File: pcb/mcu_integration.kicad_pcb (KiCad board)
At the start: 4 copper layers, 100 x 100 mm, 104 parts, among them IC1 TL7660IDGKR, IC10 AD844_OPAMP_MEL, IC2 TL081IDT, IC3 FOD814_OPTO_NOSHD, IC4 UA78M33CDCYG3, IC5 FOD814_OPTO_MEL, IC6 AD844_OPAMP_AL, IC7 FOD814_OPTO_AL, IC8 AD844_OPAMP_NOSHD, J1 Micro_SD_Card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

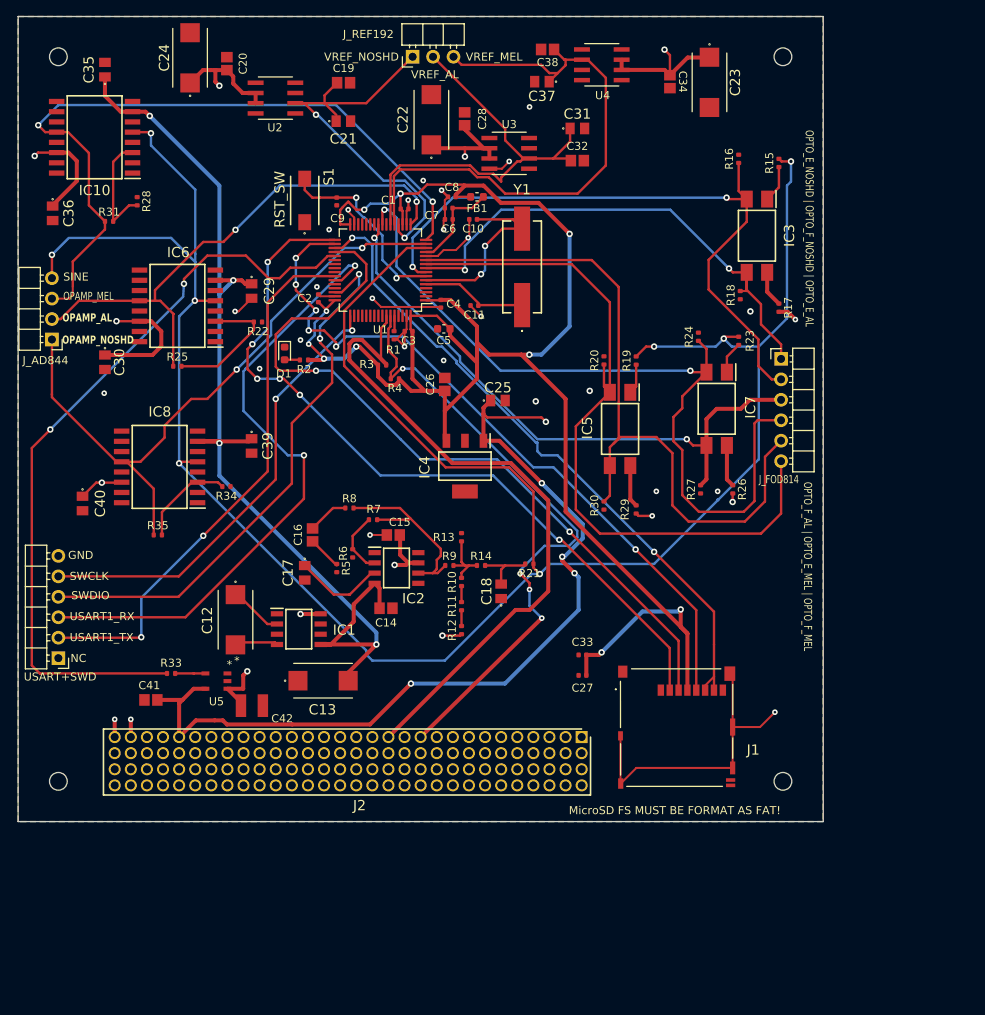
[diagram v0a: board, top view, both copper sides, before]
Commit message: Karim start 2nd rev (#16)
* done layout/ratsnet

* 95% of second rev done, just two errors
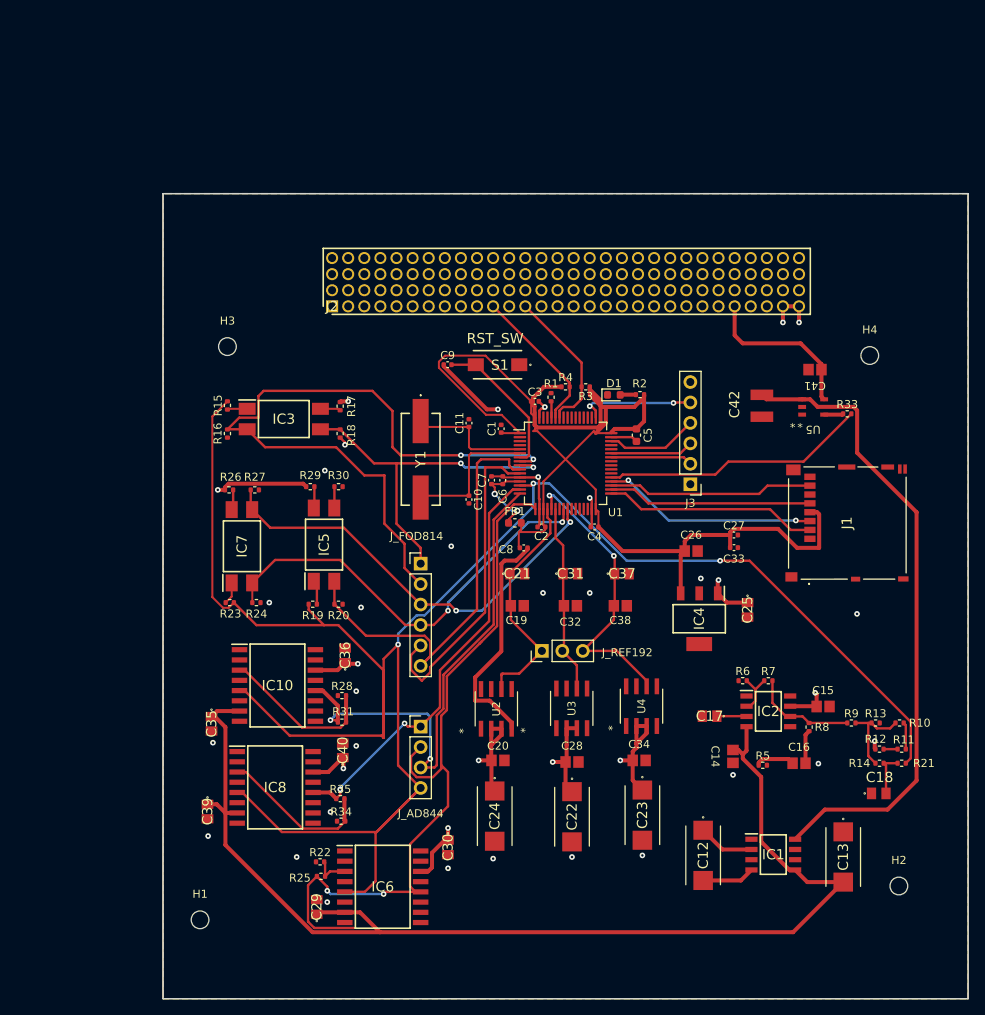
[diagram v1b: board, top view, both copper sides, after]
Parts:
- J3, J_FOD814: footprint Connector_PinHeader_2.54mm:PinHeader_1x06_P2.54mm_Horizontal -> Connector_PinHeader_2.54mm:PinHeader_1x06_P2.54mm_Vertical
- J_AD844: footprint Connector_PinHeader_2.54mm:PinHeader_1x04_P2.54mm_Horizontal -> Connector_PinHeader_2.54mm:PinHeader_1x04_P2.54mm_Vertical
- J_REF192: footprint Connector_PinHeader_2.54mm:PinHeader_1x03_P2.54mm_Horizontal -> Connector_PinHeader_2.54mm:PinHeader_1x03_P2.54mm_Vertical
- moved C24 101.5 mm to (124.2, 134.3), turned to -90 degrees
- moved C20 92.9 mm to (124.6, 127.4), turned to 0 degrees
- moved C41 92.1 mm to (164.0, 78.9)
- moved C23 91.4 mm to (142.5, 134.2)
- moved R33 90.0 mm to (168.0, 84.3), turned to 0 degrees
- moved C22 88.3 mm to (133.8, 134.4), turned to -90 degrees
- moved C34 84.4 mm to (142.1, 127.4), turned to 0 degrees
- moved C35 82.3 mm to (89.0, 122.8), turned to -90 degrees
- moved U5 81.6 mm to (163.8, 83.5), turned to 0 degrees
- moved J3 81.4 mm to (148.5, 93.1)
- moved C28 81.0 mm to (133.8, 127.6), turned to 0 degrees
- moved U2 80.7 mm to (124.4, 121.0), turned to 90 degrees
- moved U4 79.8 mm to (142.4, 120.7), turned to 90 degrees
- moved C29 76.9 mm to (102.1, 145.6), turned to 90 degrees
- moved IC6 76.5 mm to (110.3, 143.1), turned to 0 degrees
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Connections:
- C42 pad 1: +5V -> MOSFET_OUTPUT
- IC1 pad 8: +5V -> MOSFET_OUTPUT
- IC3 pad 3: GND -> ADC1_IN11_OPTO_E_NOSHD
- J1 pad 6: /SPI2_MISO -> GND
- J_FOD814 pad 1: GND -> ADC1_IN11_OPTO_E_NOSHD
- R18 pad 2: GND -> ADC1_IN11_OPTO_E_NOSHD
- U1 pad 9: GND -> ADC1_IN11_OPTO_E_NOSHD
- U5 pad 1: +5V -> MOSFET_OUTPUT
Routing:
- net +5V: track 240.4 -> 104.0 mm, vias 18 -> 11
- net GND: track 189.4 -> 67.4 mm, vias 29 -> 28
- net MOSFET_OUTPUT: track 0.00 -> 79.8 mm
- net /SPI2_CS_NSS: track 95.8 -> 26.5 mm, vias 6 -> 0
- net /USART1_RX: track 79.4 -> 10.3 mm, vias 2 -> 0
- net /SPI2_MOSI: track 94.9 -> 26.8 mm
- net OBC_I2C_SCL: track 85.4 -> 18.6 mm
- net /SPI2_SCK: track 89.8 -> 25.4 mm, vias 6 -> 0
- net MOSFET_CONTROL: track 95.3 -> 33.1 mm, vias 2 -> 0
- net OBC_I2C_SDA: track 78.4 -> 18.5 mm, vias 4 -> 0
- net 3.3V Output: track 218.9 -> 160.5 mm, vias 10 -> 0
- net /SWDIO: track 69.6 -> 11.4 mm, vias 2 -> 0
- net /USART1_TX: track 68.1 -> 10.2 mm, vias 2 -> 0
- net /SPI2_MISO: track 82.2 -> 25.5 mm, vias 2 -> 0
- net ADC1_IN13_OPTO_E_MEL: track 89.4 -> 42.5 mm
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- removed copper zone on In1.Cu, net GND
- removed copper zone on In2.Cu, net GND

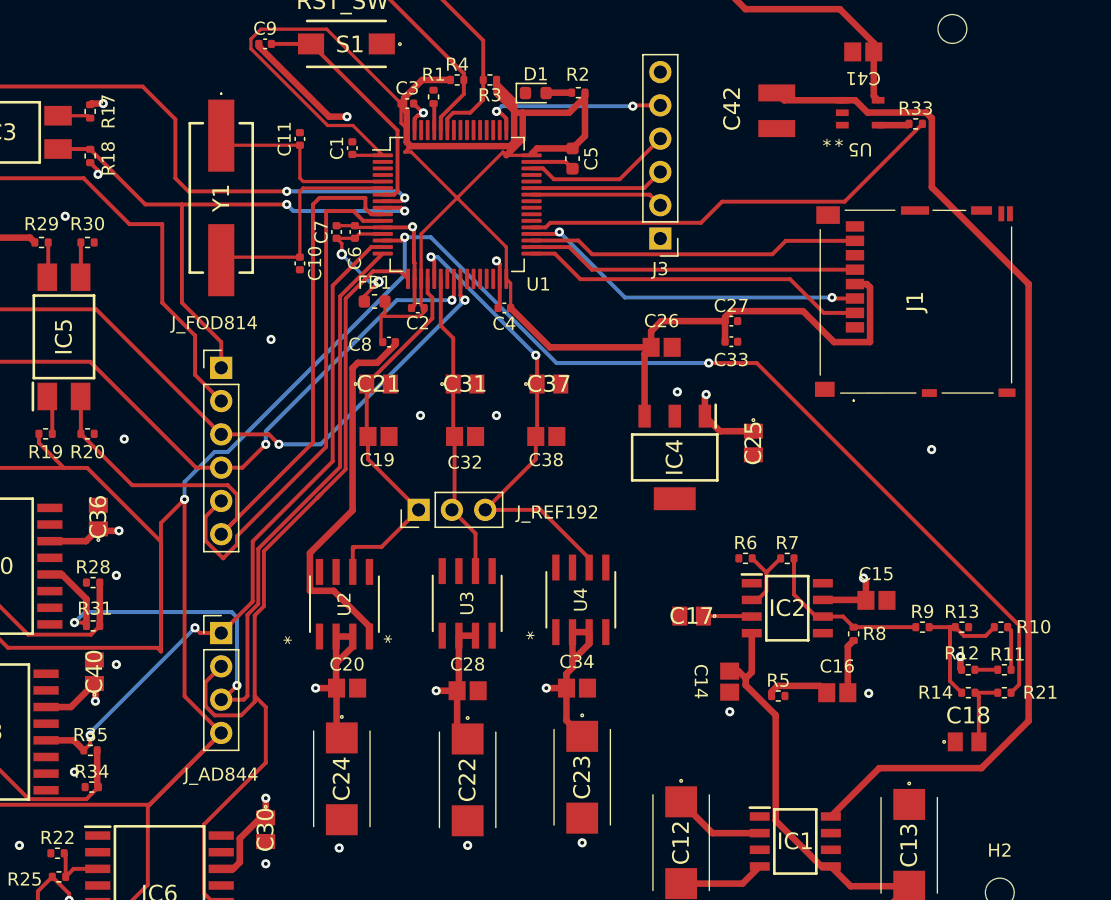
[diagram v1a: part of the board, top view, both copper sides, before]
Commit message: fix +5v connection, make final via
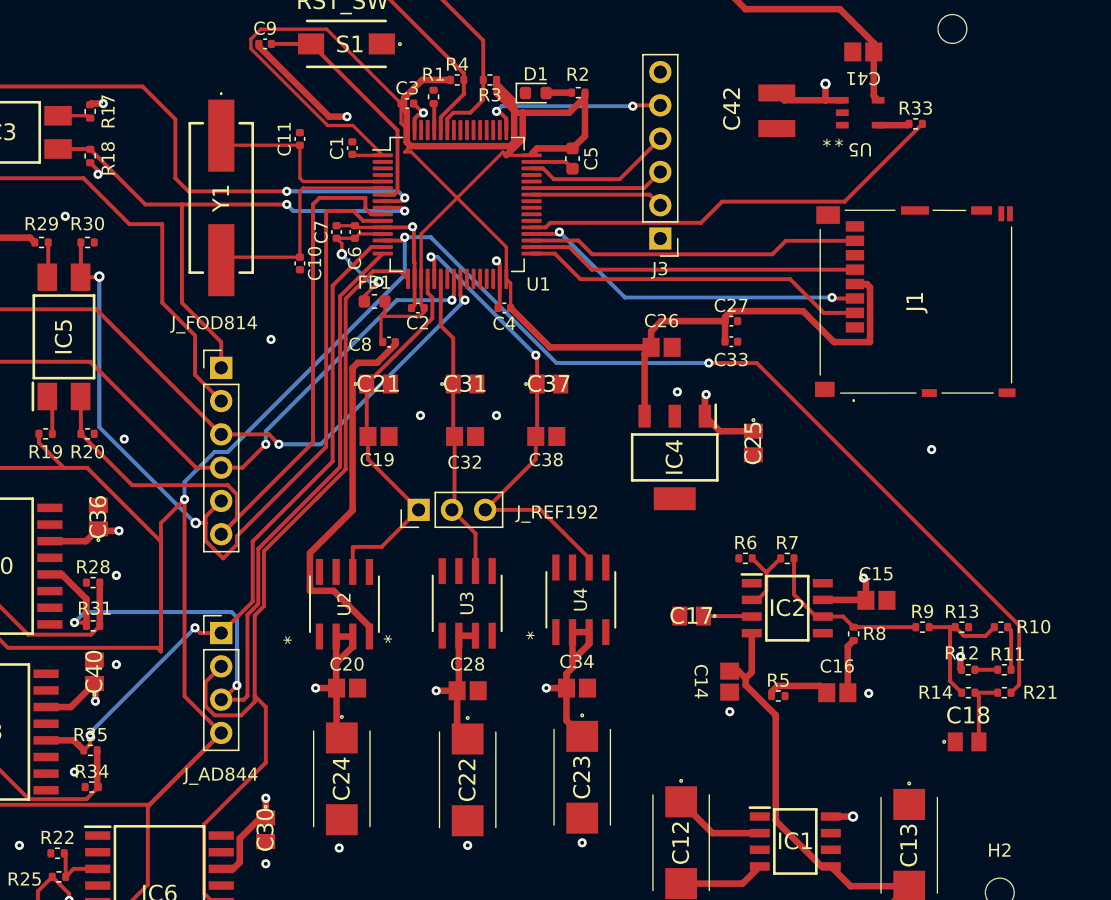
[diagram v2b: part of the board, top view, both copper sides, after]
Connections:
- C41 pad 1: +5V -> /Evan -5V and signal gen/+5V_EXT
- C42 pad 1: MOSFET_OUTPUT -> +5V
- IC1 pad 8: MOSFET_OUTPUT -> +5V
- J2 pad 26: +5V -> /Evan -5V and signal gen/+5V_EXT
- U5 pad 1: MOSFET_OUTPUT -> +5V
- U5 pad 5: +5V -> /Evan -5V and signal gen/+5V_EXT
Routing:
- net MOSFET_OUTPUT: track 79.8 -> 0.00 mm
- net ADC1_IN13_OPTO_E_MEL: track 42.5 -> 66.6 mm, vias 0 -> 2
- net /Evan -5V and signal gen/+5V_EXT: track 0.00 -> 20.4 mm
- net +5V: track 104.0 -> 91.8 mm, vias 11 -> 13

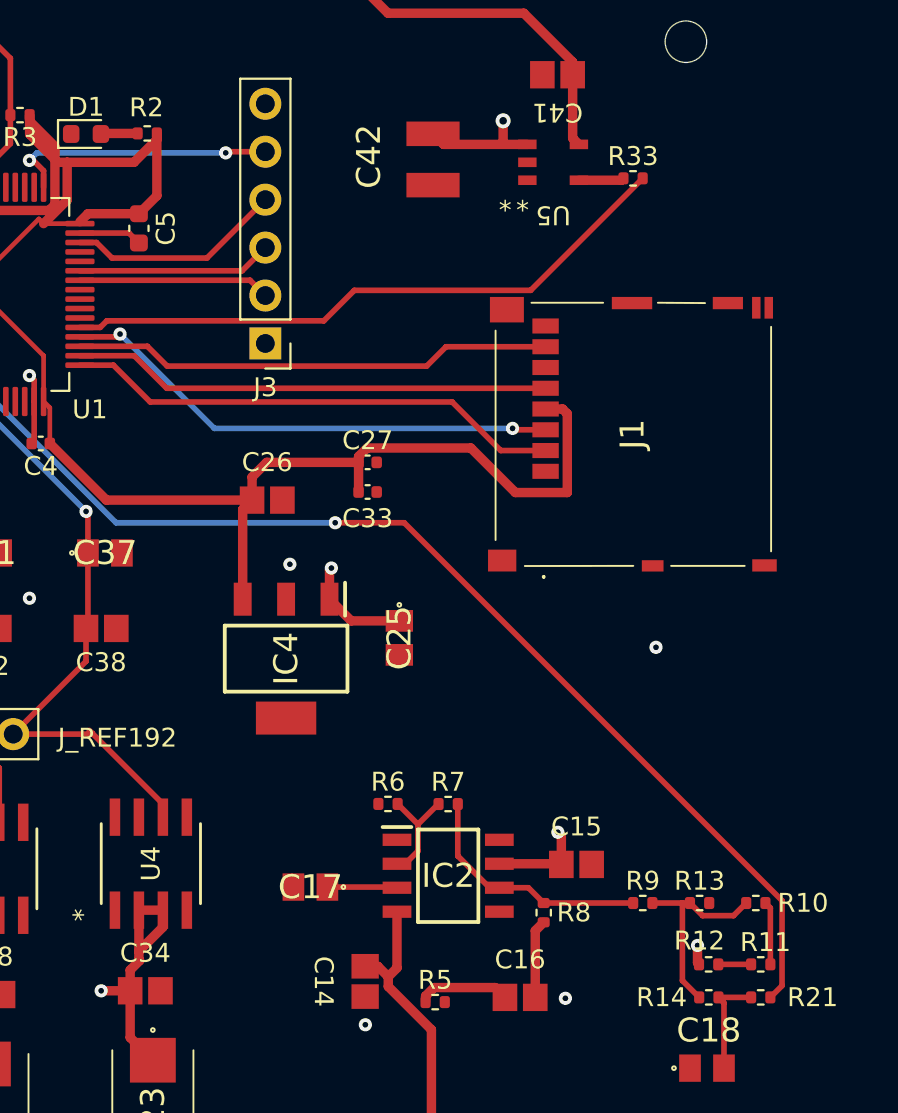
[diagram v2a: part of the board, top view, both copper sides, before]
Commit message: connect mcu 3.3vreg to +5v_ext so it always has power
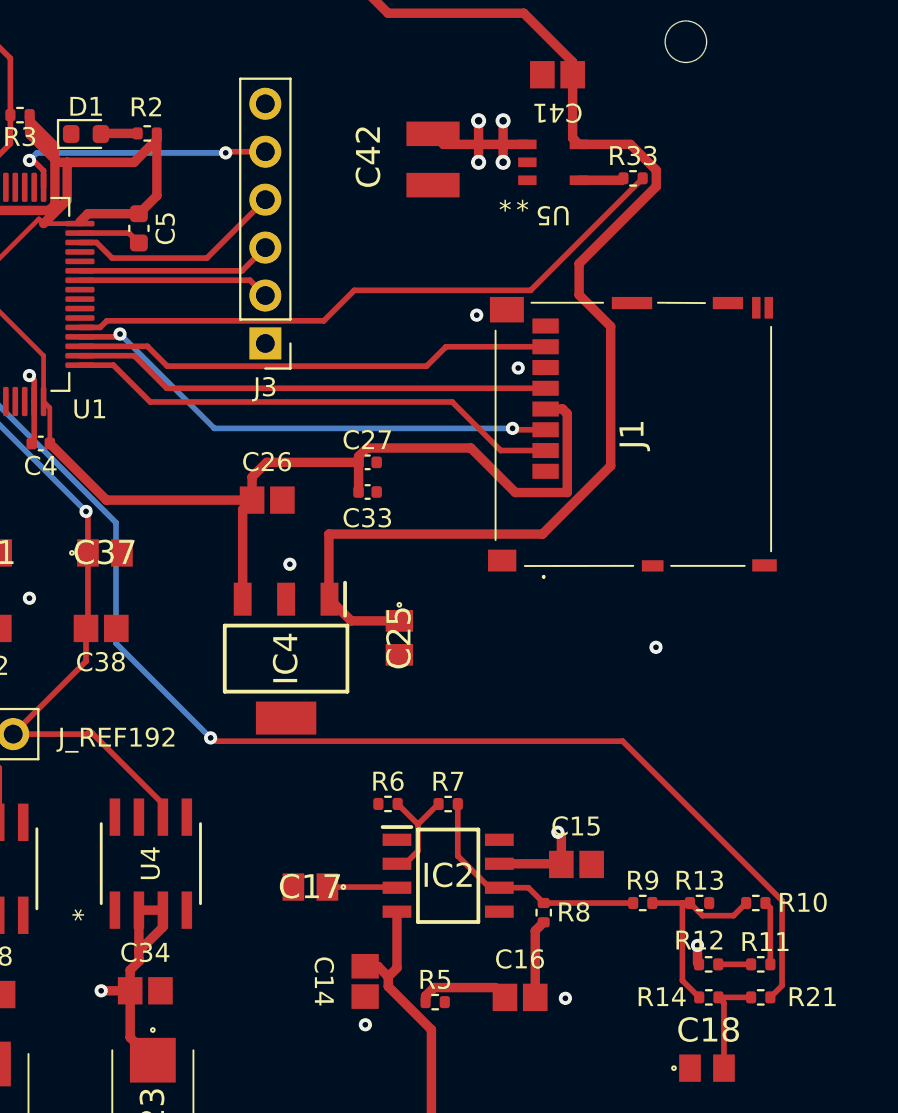
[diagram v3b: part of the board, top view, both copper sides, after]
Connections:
- C25 pad 1: +5V -> /Evan -5V and signal gen/+5V_EXT
- IC4 pad 1: +5V -> /Evan -5V and signal gen/+5V_EXT
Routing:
- net /Evan -5V and signal gen/+5V_EXT: track 20.4 -> 67.2 mm
- net ADC1_IN0_SINE: track 253.3 -> 257.1 mm
- net +5V: track 91.8 -> 89.1 mm, vias 13 -> 15
- net GND: vias 28 -> 30

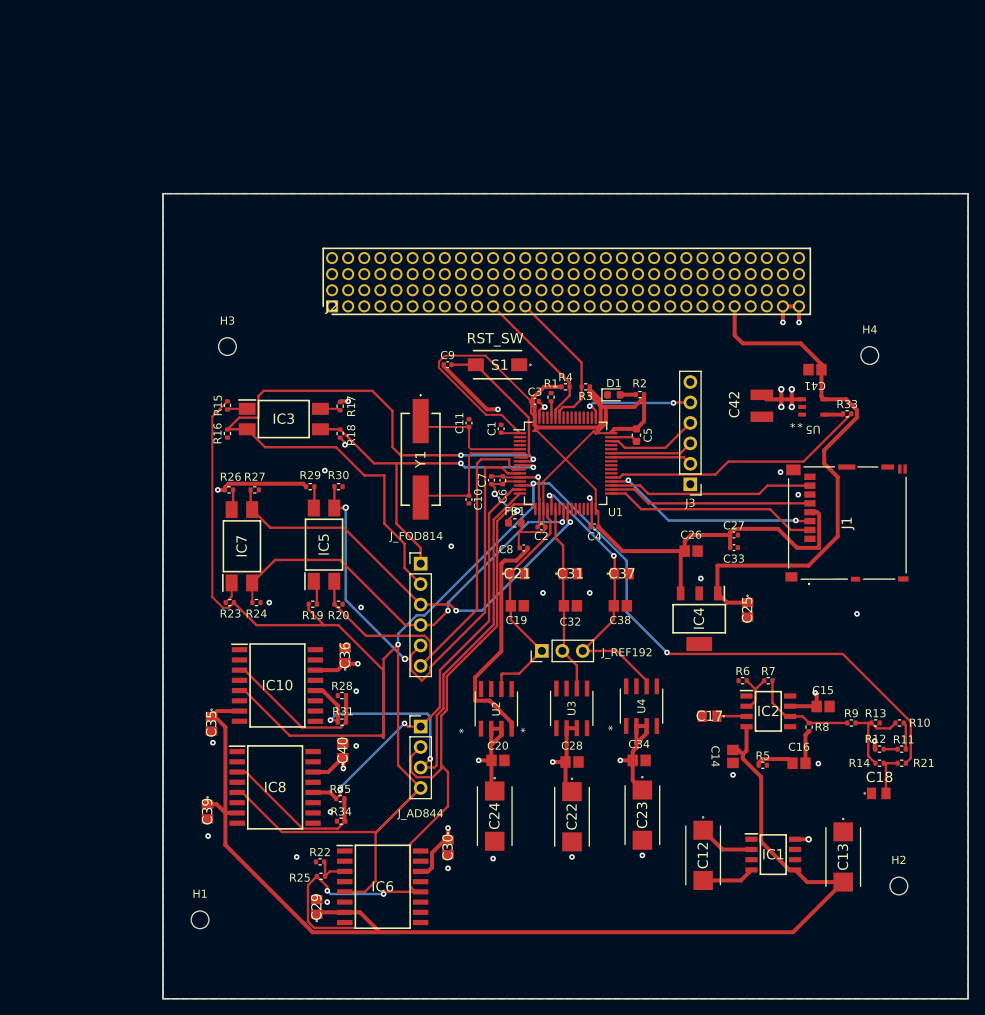
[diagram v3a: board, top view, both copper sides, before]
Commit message: fixed all errors and warnings, silk fixed
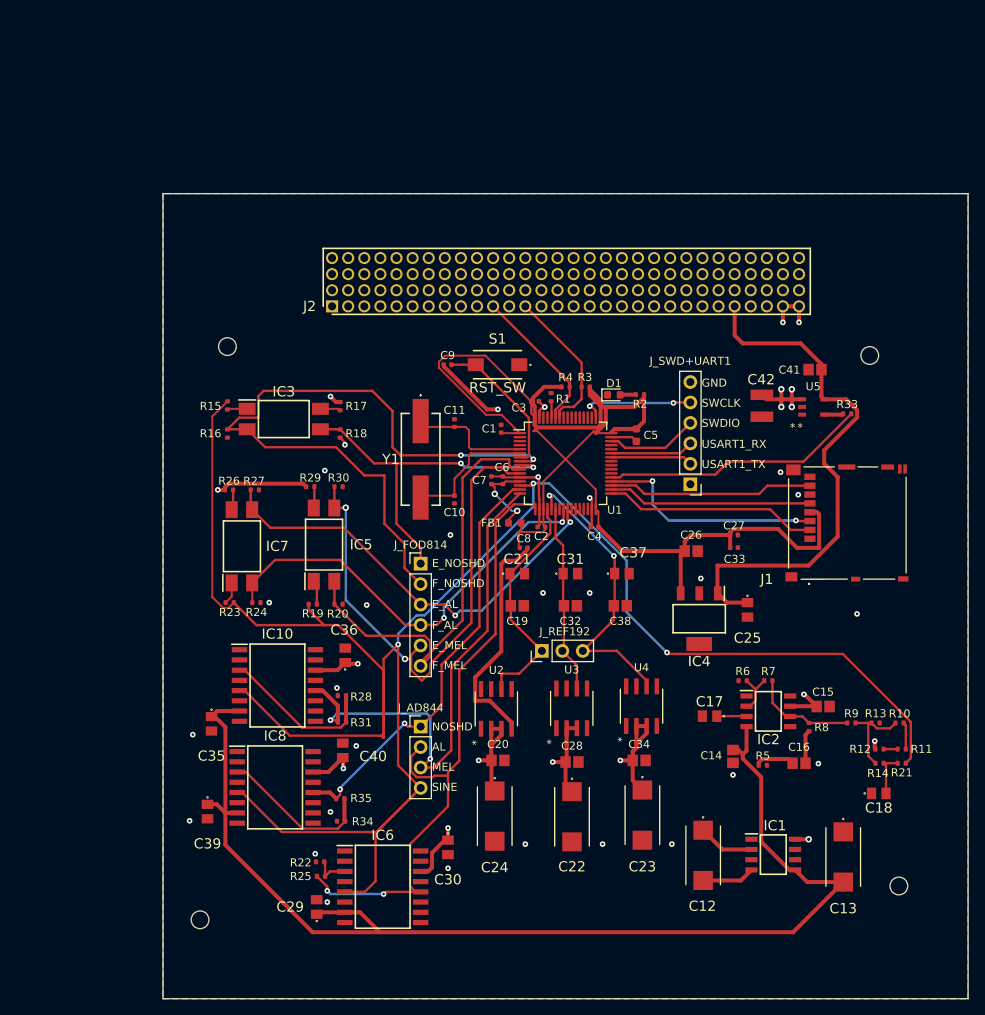
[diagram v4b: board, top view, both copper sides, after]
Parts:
- removed J3: Conn_01x06, Connector_PinHeader_2.54mm:PinHeader_1x06_P2.54mm_Vertical
- added J_SWD+UART1: Conn_01x06, Connector_PinHeader_2.54mm:PinHeader_1x06_P2.54mm_Vertical, F.Cu at (148.5, 93.1)
- moved C10 1.80 mm to (119.2, 95.0)
- moved C11 1.80 mm to (119.2, 85.5)
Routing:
- net ADC1_IN3_OPAMP_AL: track 93.2 -> 80.0 mm
- net /SPI2_MOSI: track 26.8 -> 28.5 mm
- net /HSE_OSC_OUT: track 17.5 -> 16.5 mm
- net +5V: track 89.1 -> 90.0 mm
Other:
- board text added: "AL"
- board text added: "E_AL"
- board text added: "E_MEL"
- board text added: "E_NOSHD"
- board text added: "F_AL"
- board text added: "F_MEL"
- board text added: "F_NOSHD"
- board text added: "GND"
- board text added: "MEL"
- board text added: "NOSHD"
- board text added: "SINE"
- board text added: "SWCLK"
- board text added: "SWDIO"
- board text added: "USART1_RX"
- board text added: "USART1_TX"
